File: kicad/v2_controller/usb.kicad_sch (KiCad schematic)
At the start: 33 parts, among them J1 USB_C_Receptacle_USB2.0, J2 USB_C_Receptacle_USB2.0, Q1 S8050, Q2 S8050, SW1 SW_MEC_5E, SW2 SW_MEC_5E, U2 AMS1117-3.3, U3 USBLC6-2P6, U4 USBLC6-2P6, U5 CP2102N-Axx-xQFN24

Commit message: [kicad] additional work on v2 controller
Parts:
- removed SW1, SW2: SW_MEC_5E, Button_Switch_SMD:SW_Push_1P1T_XKB_TS-1187A, symbol Switch:SW_MEC_5E
- renumbered C2 to C?, C1 to C?, D1 to D18, D2 to D19, D3 to D20, J1 to J3, J2 to J4, R6 to R10, R7 to R11, R8 to R12, R9 to R13, R10 to R14, R11 to R15, R12 to R16, R13 to R17, R2 to R6, R3 to R7, R4 to R8, R5 to R9, U2 to U4, U3 to U5, U4 to U6, U5 to U7
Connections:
- no-connect marks 18 -> 14
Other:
- note added: "LDO"
- note added: "UART-to-USB"
- note added: "USB Connectors"
- moved on the sheet: C?, D18, J3, Q1, Q2, R11, R12, R13, R14, R15, R16, R17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

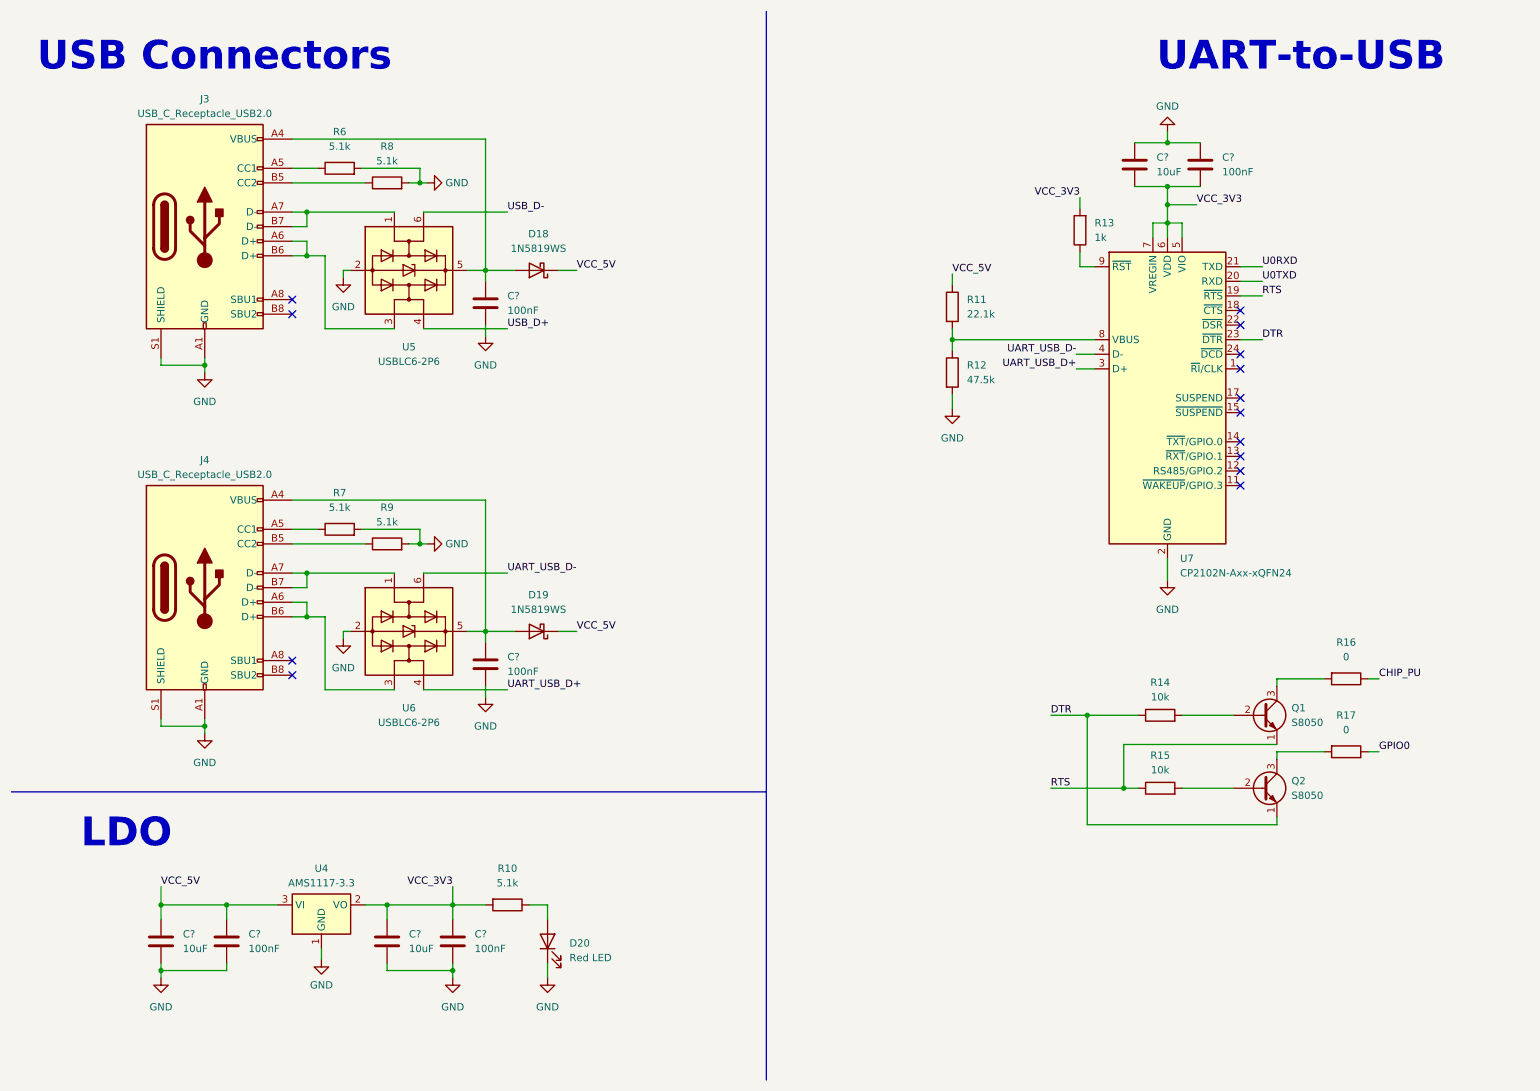
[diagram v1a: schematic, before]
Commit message: [kicad] fix global symbol usage in v2 controller
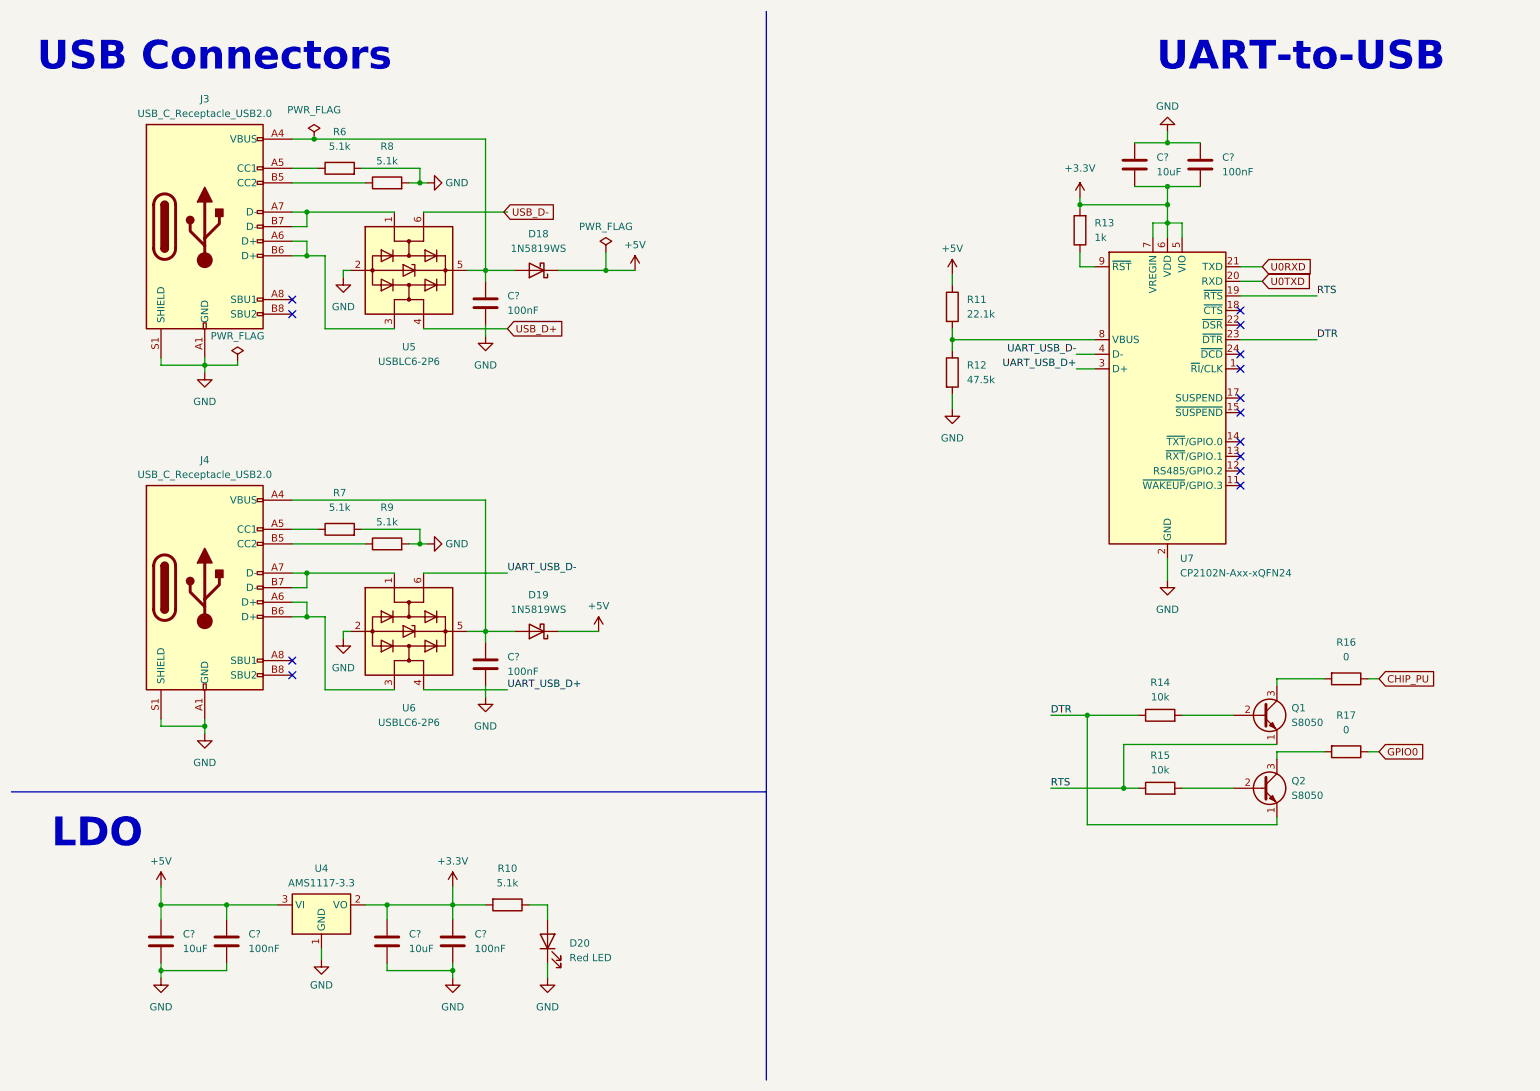
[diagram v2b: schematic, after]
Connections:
- net VCC_3V3 renamed +3.3V
- net VCC_5V renamed +5V

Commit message: [kicad] update v2 controller to use hierarchical labels
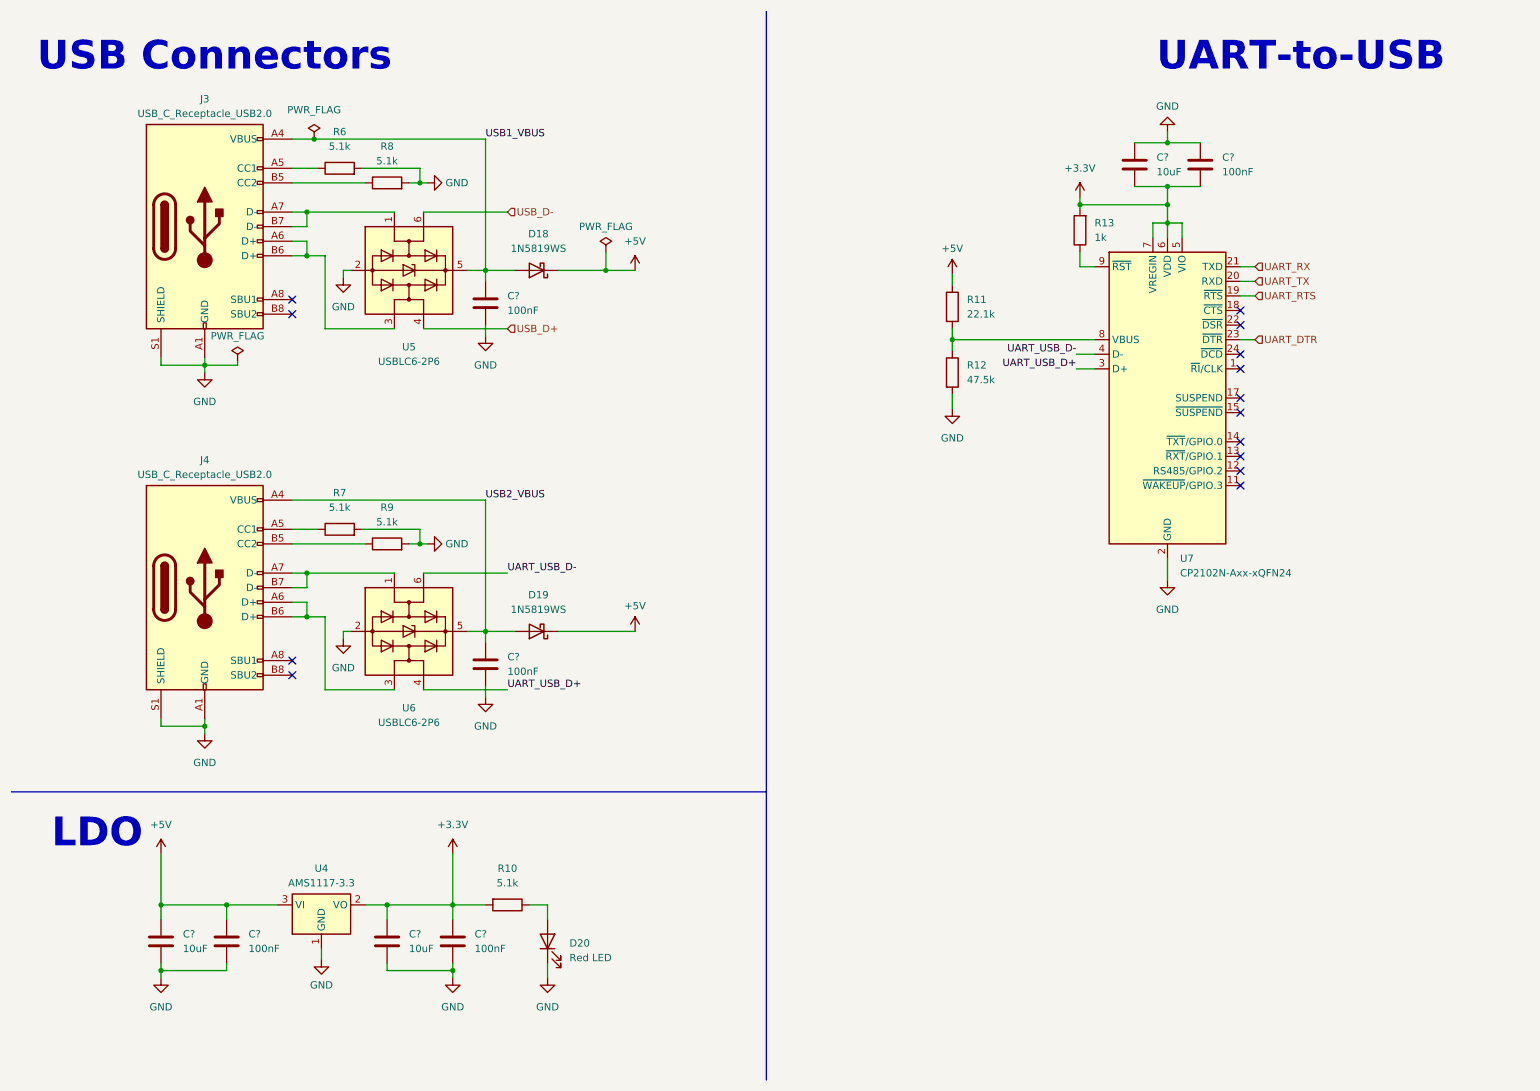
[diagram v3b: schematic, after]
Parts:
- removed Q1, Q2: S8050, Package_TO_SOT_SMD:SOT-23, symbol Transistor_BJT:S8050
- removed R14, R15: 10k, Resistor_SMD:R_0402_1005Metric, symbol Device:R
- removed R16, R17: 0, Resistor_SMD:R_0402_1005Metric, symbol Device:R
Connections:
- net USB1_VBUS: now reaches C?.1, D18.2 (A), J3.A4 (VBUS), J3.A9 (VBUS), J3.B4 (VBUS), J3.B9 (VBUS), U5.5 (VBUS)
- net USB2_VBUS: now reaches C?.1, D19.2 (A), J4.A4 (VBUS), J4.A9 (VBUS), J4.B4 (VBUS), J4.B9 (VBUS), U6.5 (VBUS)
- net DTR renamed UART_DTR
- net RTS renamed UART_RTS
- net U0RXD renamed UART_RX
- net U0TXD renamed UART_TX

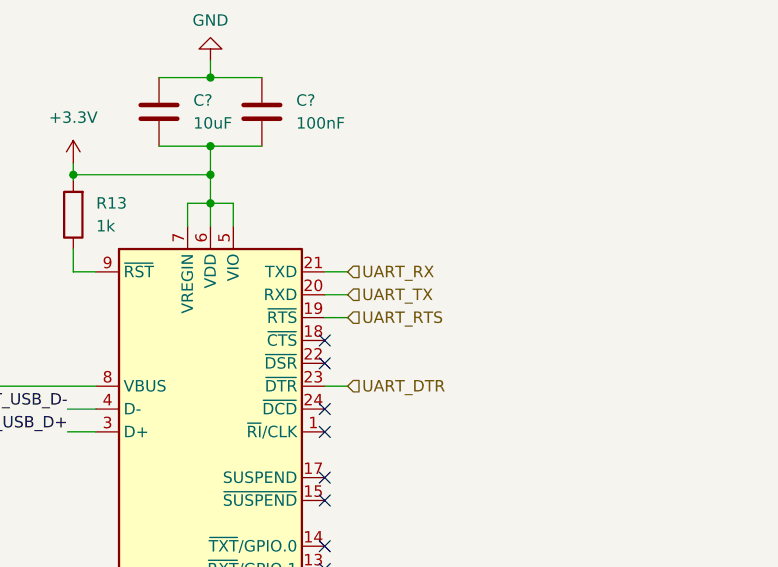
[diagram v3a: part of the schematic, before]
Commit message: [kicad] add a debug header to the v2 controller
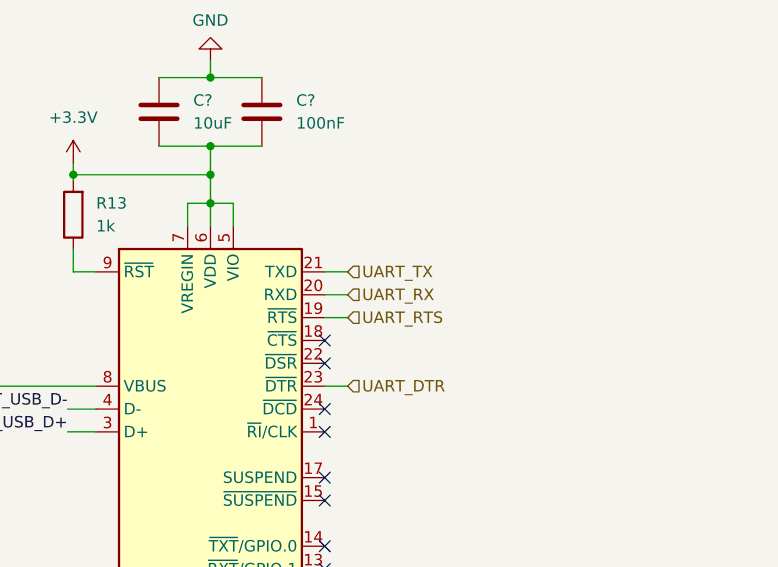
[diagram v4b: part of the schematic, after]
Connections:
- net UART_RX: now also U7.20 (RXD); no longer U7.21 (TXD)
- net UART_TX: now also U7.21 (TXD); no longer U7.20 (RXD)
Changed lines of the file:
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@@
     (effects (font (size 1.27 1.27)) (justify left))
   )
-  (hierarchical_label "UART_RX" (shape input) (at 228.6 56.515 0) (fields_autoplaced)
+  (hierarchical_label "UART_TX" (shape input) (at 228.6 56.515 0) (fields_autoplaced)
     (effects (font (size 1.27 1.27)) (justify left))
   )
@@
     (effects (font (size 1.27 1.27)) (justify left))
   )
-  (hierarchical_label "UART_TX" (shape input) (at 228.6 59.055 0) (fields_autoplaced)
+  (hierarchical_label "UART_RX" (shape input) (at 228.6 59.055 0) (fields_autoplaced)
     (effects (font (size 1.27 1.27)) (justify left))
   )

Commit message: [kicad] use vertical USB-C receptacles
There isn't enough space around the edges of the board for horizontal
mount receptacles.
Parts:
- J3, J4: footprint Connector_USB:USB_C_Receptacle_Molex_105450-0101 -> Connector_USB:USB_C_Receptacle_G-Switch_GT-USB-7051x; LCSC Part # C134092 -> C2843970
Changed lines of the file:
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@@
       (effects (font (size 1.27 1.27)))
     )
-    (property "Footprint" "Connector_USB:USB_C_Receptacle_Molex_105450-0101" (at 49.53 49.53 0)
-      (effects (font (size 1.27 1.27)) hide)
-    )
-    (property "Datasheet" "https://www.usb.org/sites/default/files/documents/usb_type-c.zip" (at 49.53 49.53 0)
-      (effects (font (size 1.27 1.27)) hide)
-    )
-    (property "LCSC Part #" "C134092" (at 45.72 49.53 0)
+    (property "Footprint" "Connector_USB:USB_C_Receptacle_G-Switch_GT-USB-7051x" (at 49.53 49.53 0)
+      (effects (font (size 1.27 1.27)) hide)
+    )
+    (property "Datasheet" "https://datasheet.lcsc.com/lcsc/2108072030_G-Switch-GT-USB-7051A_C2843970.pdf" (at 49.53 49.53 0)
+      (effects (font (size 1.27 1.27)) hide)
+    )
+    (property "LCSC Part #" "C2843970" (at 45.72 49.53 0)
       (effects (font (size 1.27 1.27)) hide)
     )
@@
       (effects (font (size 1.27 1.27)))
     )
-    (property "Footprint" "Connector_USB:USB_C_Receptacle_Molex_105450-0101" (at 49.53 112.395 0)
-      (effects (font (size 1.27 1.27)) hide)
-    )
-    (property "Datasheet" "https://www.usb.org/sites/default/files/documents/usb_type-c.zip" (at 49.53 112.395 0)
-      (effects (font (size 1.27 1.27)) hide)
-    )
-    (property "LCSC Part #" "C134092" (at 45.72 112.395 0)
-      (effects (font (size 1.27 1.27)) hide)
-    )
+    (property "Footprint" "Connector_USB:USB_C_Receptacle_G-Switch_GT-USB-7051x" (at 49.53 112.395 0)
+      (effects (font (size 1.27 1.27)) hide)
+    )
+    (property "Datasheet" "https://datasheet.lcsc.com/lcsc/2108072030_G-Switch-GT-USB-7051A_C2843970.pdf" (at 49.53 112.395 0)
+      (effects (font (size 1.27 1.27)) hide)
+    )
+    (property "LCSC Part #" "C2843970" (at 45.72 112.395 0)
+      (effects (font (size 1.27 1.27)) hide)
+    )

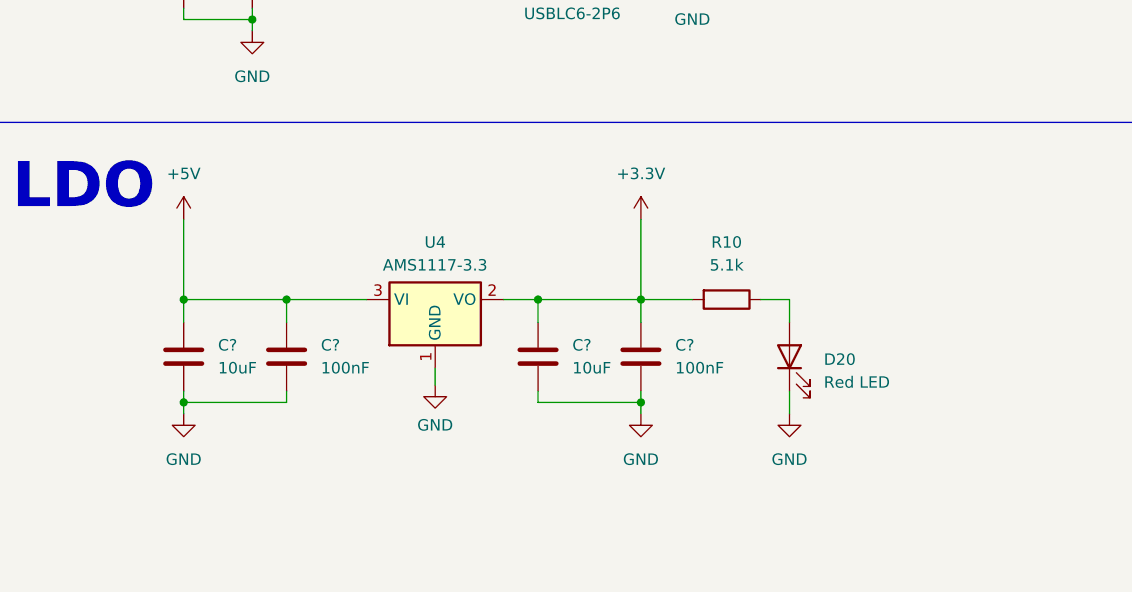
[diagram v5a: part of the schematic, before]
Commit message: [kicad] swap LDO from AMS1117 to NXP167BMX330TBG
I originally used AMS1117 since it is available as a basic part from
JLCPCB.  However, it requires a 22uF tantalum capacitor on the output,
which is only available as extended part, negating the cost savings of
the basic part.

This switches to using the NXP167BMX330TBG chip instead, which has much
lower quiescent current draw, higher PSRR, and a smaller footprint.  It
is only rated for 700mA, compared to 1A for the AMS1117, but my board
generally shouldn't be drawing that much power through the 3.3V lines.
The maximum allowed current draw for USB 2.0 is only 500mA.  The LEDs
are also probably the highest current draw, and these are powered
directly from 5V rather than the LDO's 3.3V output.
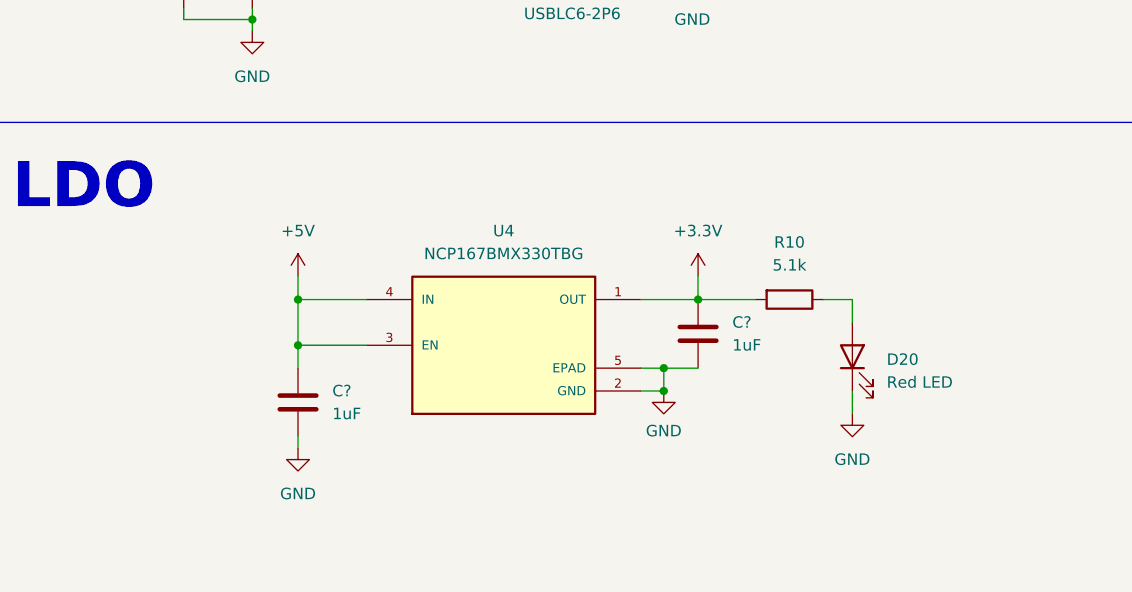
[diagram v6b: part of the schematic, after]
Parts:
- removed C? (x2): 10uF, Capacitor_SMD:C_0603_1608Metric, symbol Device:C
- removed C? (x2): 100nF, Capacitor_SMD:C_0402_1005Metric, symbol Device:C
- removed U4: AMS1117-3.3, Package_TO_SOT_SMD:SOT-223-3_TabPin2, symbol Regulator_Linear:AMS1117-3.3
- added C? (x2): 1uF, Capacitor_SMD:C_0402_1005Metric, symbol Device:C
- added U4: NCP167BMX330TBG, Package_DFN_QFN:OnSemi_XDFN4-1EP_1.0x1.0mm_EP0.52x0.52mm, symbol mantyl:NCP167BMX330TBG
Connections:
- net +3.3V: now also C?.1, U4.1 (OUT)
- net +5V: now also C?.1, U4.3 (EN), U4.4 (IN)
- net GND: now also C?.2, C?.2, U4.2 (GND), U4.5 (EPAD)
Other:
- moved on the sheet: D20, R10
